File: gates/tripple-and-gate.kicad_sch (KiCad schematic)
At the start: 0 parts

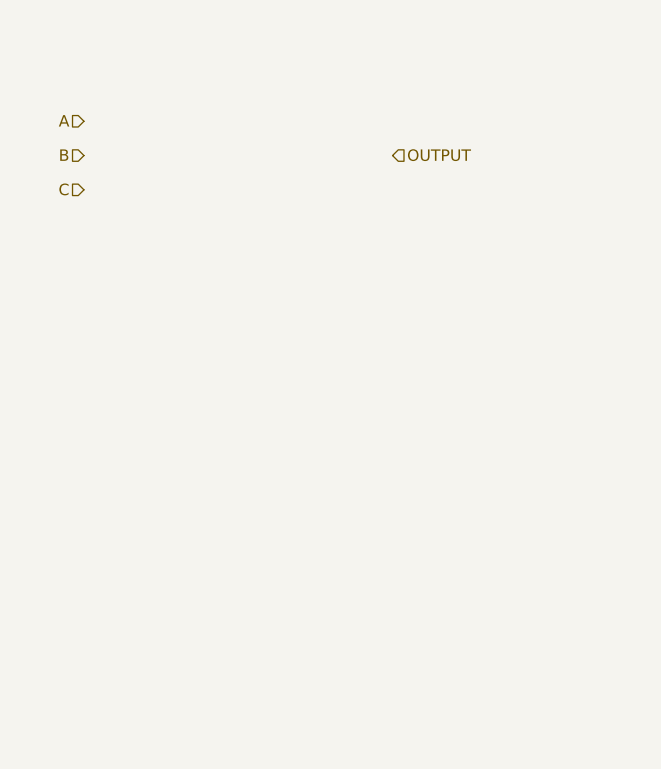
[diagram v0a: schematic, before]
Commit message: Alternative and gates with different amounts of inputs
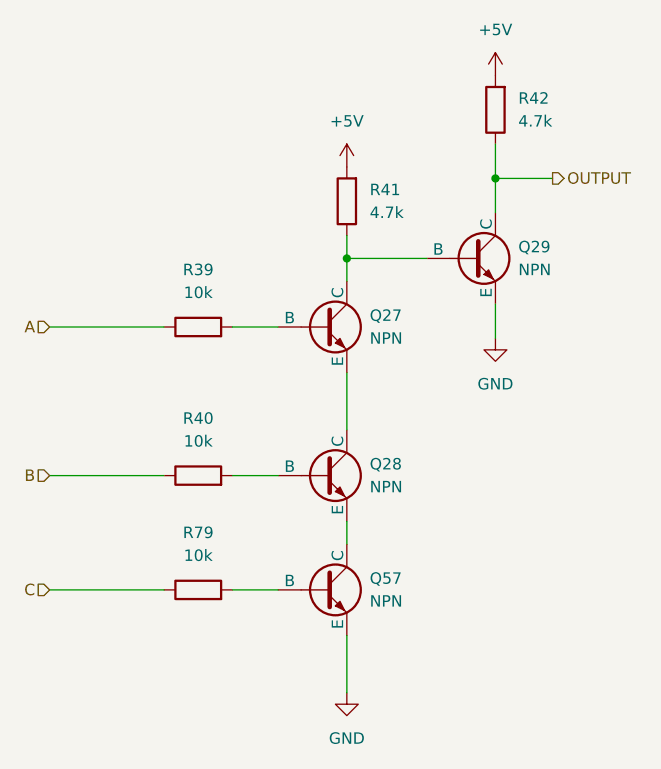
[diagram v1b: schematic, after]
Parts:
- added Q27, Q28, Q29, Q57: NPN, SOT-23-3_L2.9-W1.6-P1.90-LS2.8-BR:SOT-23-3_L2.9-W1.6-P1.90-LS2.8-BR, symbol Simulation_SPICE:NPN
- added R39, R40, R79: 10k, R0603:R0603, symbol Device:R
- added R41, R42: 4.7k, R0603:R0603, symbol Device:R
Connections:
- net A: now also R39.1
- net B: now also R40.1
- net C: now also R79.1
- net OUTPUT: now also Q29.1 (C), R42.1
- new net: Q27.1 (C), Q29.2 (B), R41.1
- new net: Q57.2 (B), R79.2
- new net: Q28.2 (B), R40.2
- new net: Q27.2 (B), R39.2
- new net: Q27.3 (E), Q28.1 (C)
- new net: Q28.3 (E), Q57.1 (C)
- new net +5V: R41.2, R42.2
- new net GND: Q29.3 (E), Q57.3 (E)

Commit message: complete 2-bit encoder
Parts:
- renumbered Q27 to Q46, Q28 to Q47, Q57 to Q48, Q29 to Q49, R39 to R61, R40 to R62, R79 to R63, R41 to R64, R42 to R65
